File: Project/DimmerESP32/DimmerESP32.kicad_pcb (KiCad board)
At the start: 2 copper layers, 78.7 x 58.4 mm, 14 parts, among them J1 Conn_01x05_Male, J2 Conn_01x04_Male, Q1 BT136-600, U1 MOC3021M, U2 4N25

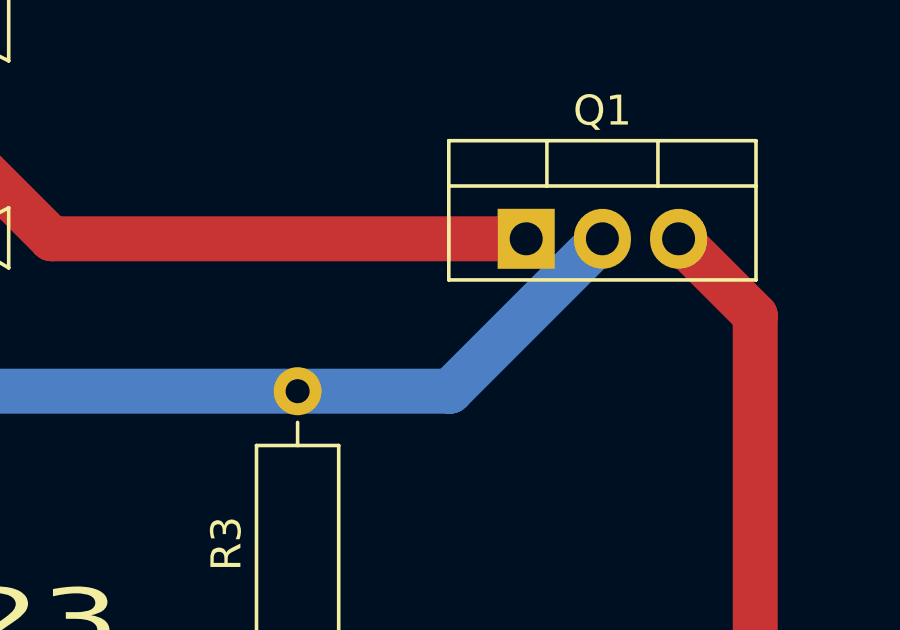
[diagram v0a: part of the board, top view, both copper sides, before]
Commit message: Change 4N25 to TIL111
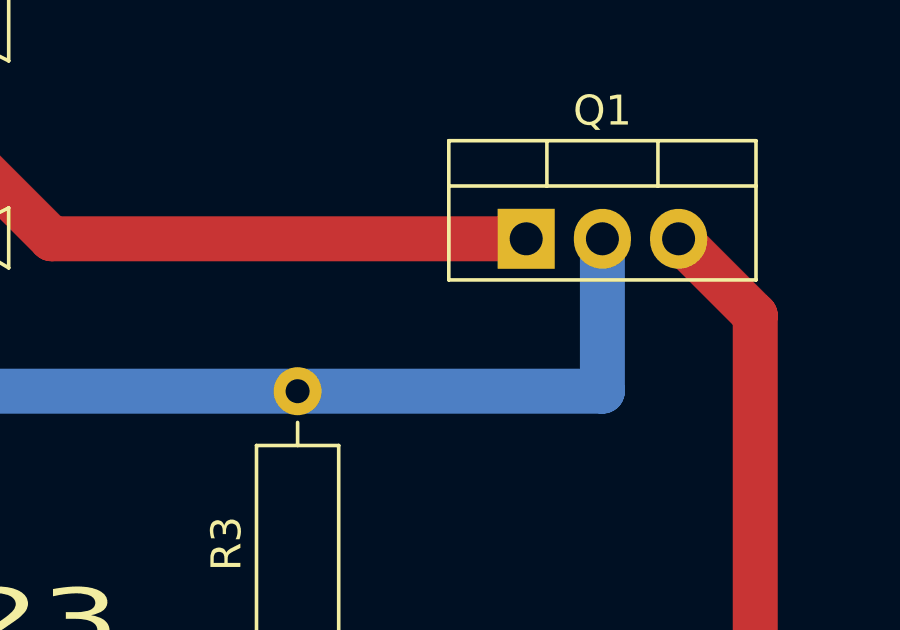
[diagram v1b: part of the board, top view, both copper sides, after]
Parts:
- U2: value 4N25 -> TIL111
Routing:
- net Net-(GridIN1-Pad1): track 76.4 -> 79.4 mm
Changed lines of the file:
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@@
-    )
-  )
-  (footprint "Package_DIP:DIP-6_W7.62mm" (layer "F.Cu")
-    (at 125.74 104.155)
-    (descr "6-lead though-hole mounted DIP package, row spacing 7.62 mm (300 mils)")
-    (tags "THT DIP DIL PDIP 2.54mm 7.62mm 300mil")
-    (property "Sheetfile" "DimmerESP32.kicad_sch")
-    (property "Sheetname" "")
-    (attr through_hole)
-    (fp_text reference "U2" (at 3.81 -2.33) (layer "F.SilkS")
-      (effects (font (size 1 1) (thickness 0.15)))
-    )
-    (fp_text value "4N25" (at 3.81 7.41) (layer "F.Fab")
-      (effects (font (size 1 1) (thickness 0.15)))
-    )
-    (fp_text user "${REFERENCE}" (at 3.81 2.54) (layer "F.Fab")
-      (effects (font (size 1 1) (thickness 0.15)))
-    )
-    (fp_line (start 6.46 6.41) (end 6.46 -1.33) (layer "F.SilkS") (width 0.12))
-    (fp_line (start 2.81 -1.33) (end 1.16 -1.33) (layer "F.SilkS") (width 0.12))
-    (fp_line (start 1.16 6.41) (end 6.46 6.41) (layer "F.SilkS") (width 0.12))
-    (fp_line (start 6.46 -1.33) (end 4.81 -1.33) (layer "F.SilkS") (width 0.12))
-    (fp_line (start 1.16 -1.33) (end 1.16 6.41) (layer "F.SilkS") (width 0.12))
-    (fp_arc (start 4.81 -1.33) (mid 3.81 -0.33) (end 2.81 -1.33) (layer "F.SilkS") (width 0.12))
-    (fp_line (start 8.7 6.6) (end 8.7 -1.55) (layer "F.CrtYd") (width 0.05))
-    (fp_line (start -1.1 6.6) (end 8.7 6.6) (layer "F.CrtYd") (width 0.05))
-    (fp_line (start -1.1 -1.55) (end -1.1 6.6) (layer "F.CrtYd") (width 0.05))
-    (fp_line (start 8.7 -1.55) (end -1.1 -1.55) (layer "F.CrtYd") (width 0.05))
-    (fp_line (start 0.635 -0.27) (end 1.635 -1.27) (layer "F.Fab") (width 0.1))
-    (fp_line (start 6.985 6.35) (end 0.635 6.35) (layer "F.Fab") (width 0.1))
-    (fp_line (start 1.635 -1.27) (end 6.985 -1.27) (layer "F.Fab") (width 0.1))
-    (fp_line (start 0.635 6.35) (end 0.635 -0.27) (layer "F.Fab") (width 0.1))
-    (fp_line (start 6.985 -1.27) (end 6.985 6.35) (layer "F.Fab") (width 0.1))
-    (pad "1" thru_hole rect (at 0 0) (size 1.6 1.6) (drill 0.8) (layers *.Cu *.Mask)
-      (net 1 "Net-(D2-Pad1)") (pintype "passive"))
-    (pad "2" thru_hole oval (at 0 2.54) (size 1.6 1.6) (drill 0.8) (layers *.Cu *.Mask)
-      (net 3 "Net-(D2-Pad3)") (pintype "passive"))
-    (pad "3" thru_hole oval (at 0 5.08) (size 1.6 1.6) (drill 0.8) (layers *.Cu *.Mask)
-      (net 13 "unconnected-(U2-Pad3)") (pinfunction "NC") (pintype "no_connect"))
-    (pad "4" thru_hole oval (at 7.62 5.08) (size 1.6 1.6) (drill 0.8) (layers *.Cu *.Mask)
-      (net 14 "GND") (pintype "passive"))
-    (pad "5" thru_hole oval (at 7.62 2.54) (size 1.6 1.6) (drill 0.8) (layers *.Cu *.Mask)
-      (net 15 "ZeroCrossing") (pintype "passive"))
-    (pad "6" thru_hole oval (at 7.62 0) (size 1.6 1.6) (drill 0.8) (layers *.Cu *.Mask)
-      (net 16 "unconnected-(U2-Pad6)") (pintype "passive"))
-    (model "${KICAD6_3DMODEL_DIR}/Package_DIP.3dshapes/DIP-6_W7.62mm.wrl"
-      (offset (xyz 0 0 0))
-      (scale (xyz 1 1 1))
-      (rotate (xyz 0 0 0))
     )
   )
@@
     )
   )
+  (footprint "Package_DIP:DIP-6_W7.62mm" (layer "F.Cu")
+    (at 125.74 104.155)
+    (descr "6-lead though-hole mounted DIP package, row spacing 7.62 mm (300 mils)")
+    (tags "THT DIP DIL PDIP 2.54mm 7.62mm 300mil")
+    (property "Sheetfile" "DimmerESP32.kicad_sch")
+    (property "Sheetname" "")
+    (attr through_hole)
+    (fp_text reference "U2" (at 3.81 -2.33) (layer "F.SilkS")
+      (effects (font (size 1 1) (thickness 0.15)))
+    )
+    (fp_text value "TIL111" (at 3.81 7.41) (layer "F.Fab")
+      (effects (font (size 1 1) (thickness 0.15)))
+    )
+    (fp_text user "${REFERENCE}" (at 3.81 2.54) (layer "F.Fab")
+      (effects (font (size 1 1) (thickness 0.15)))
+    )
+    (fp_line (start 1.16 6.41) (end 6.46 6.41) (layer "F.SilkS") (width 0.12))
+    (fp_line (start 6.46 6.41) (end 6.46 -1.33) (layer "F.SilkS") (width 0.12))
+    (fp_line (start 1.16 -1.33) (end 1.16 6.41) (layer "F.SilkS") (width 0.12))
+    (fp_line (start 2.81 -1.33) (end 1.16 -1.33) (layer "F.SilkS") (width 0.12))
+    (fp_line (start 6.46 -1.33) (end 4.81 -1.33) (layer "F.SilkS") (width 0.12))
+    (fp_arc (start 4.81 -1.33) (mid 3.81 -0.33) (end 2.81 -1.33) (layer "F.SilkS") (width 0.12))
+    (fp_line (start -1.1 6.6) (end 8.7 6.6) (layer "F.CrtYd") (width 0.05))
+    (fp_line (start 8.7 6.6) (end 8.7 -1.55) (layer "F.CrtYd") (width 0.05))
+    (fp_line (start -1.1 -1.55) (end -1.1 6.6) (layer "F.CrtYd") (width 0.05))
+    (fp_line (start 8.7 -1.55) (end -1.1 -1.55) (layer "F.CrtYd") (width 0.05))
+    (fp_line (start 6.985 -1.27) (end 6.985 6.35) (layer "F.Fab") (width 0.1))
+    (fp_line (start 0.635 6.35) (end 0.635 -0.27) (layer "F.Fab") (width 0.1))
+    (fp_line (start 0.635 -0.27) (end 1.635 -1.27) (layer "F.Fab") (width 0.1))
+    (fp_line (start 6.985 6.35) (end 0.635 6.35) (layer "F.Fab") (width 0.1))
+    (fp_line (start 1.635 -1.27) (end 6.985 -1.27) (layer "F.Fab") (width 0.1))
+    (pad "1" thru_hole rect (at 0 0) (size 1.6 1.6) (drill 0.8) (layers *.Cu *.Mask)
+      (net 1 "Net-(D2-Pad1)") (pintype "passive"))
+    (pad "2" thru_hole oval (at 0 2.54) (size 1.6 1.6) (drill 0.8) (layers *.Cu *.Mask)
+      (net 3 "Net-(D2-Pad3)") (pintype "passive"))
+    (pad "3" thru_hole oval (at 0 5.08) (size 1.6 1.6) (drill 0.8) (layers *.Cu *.Mask)
+      (net 13 "unconnected-(U2-Pad3)") (pinfunction "NC") (pintype "no_connect"))
+    (pad "4" thru_hole oval (at 7.62 5.08) (size 1.6 1.6) (drill 0.8) (layers *.Cu *.Mask)
+      (net 14 "GND") (pintype "passive"))
+    (pad "5" thru_hole oval (at 7.62 2.54) (size 1.6 1.6) (drill 0.8) (layers *.Cu *.Mask)
+      (net 15 "ZeroCrossing") (pintype "passive"))
+    (pad "6" thru_hole oval (at 7.62 0) (size 1.6 1.6) (drill 0.8) (layers *.Cu *.Mask)
+      (net 16 "unconnected-(U2-Pad6)") (pintype "passive"))
+    (model "${KICAD6_3DMODEL_DIR}/Package_DIP.3dshapes/DIP-6_W7.62mm.wrl"
+      (offset (xyz 0 0 0))
+      (scale (xyz 1 1 1))
+      (rotate (xyz 0 0 0))
+    )
+  )
   (gr_rect (start 182.88 92.695) (end 129.55 114.3) (layer "F.SilkS") (width 0.15) (fill none))
   (gr_rect (start 104.14 55.88) (end 182.88 114.3) (layer "Edge.Cuts") (width 0.1) (fill none))
@@
   (segment (start 109.3 63.9) (end 109.3 76.12) (width 1.5) (layer "F.Cu") (net 11))
   (segment (start 109.3 76.12) (end 109.22 76.2) (width 0.25) (layer "F.Cu") (net 11))
-  (segment (start 160.02 73.66) (end 165.1 73.66) (width 1.5) (layer "B.Cu") (net 11))
+  (segment (start 170.18 73.66) (end 170.18 68.58) (width 1.5) (layer "B.Cu") (net 11))
+  (segment (start 160.02 73.66) (end 170.18 73.66) (width 1.5) (layer "B.Cu") (net 11))
   (segment (start 109.22 76.2) (end 111.76 73.66) (width 1.5) (layer "B.Cu") (net 11))
-  (segment (start 165.1 73.66) (end 170.18 68.58) (width 1.5) (layer "B.Cu") (net 11))
   (segment (start 111.76 73.66) (end 160.02 73.66) (width 1.5) (layer "B.Cu") (net 11))
   (segment (start 175.275 71.135) (end 172.72 68.58) (width 1.5) (layer "F.Cu") (net 12))

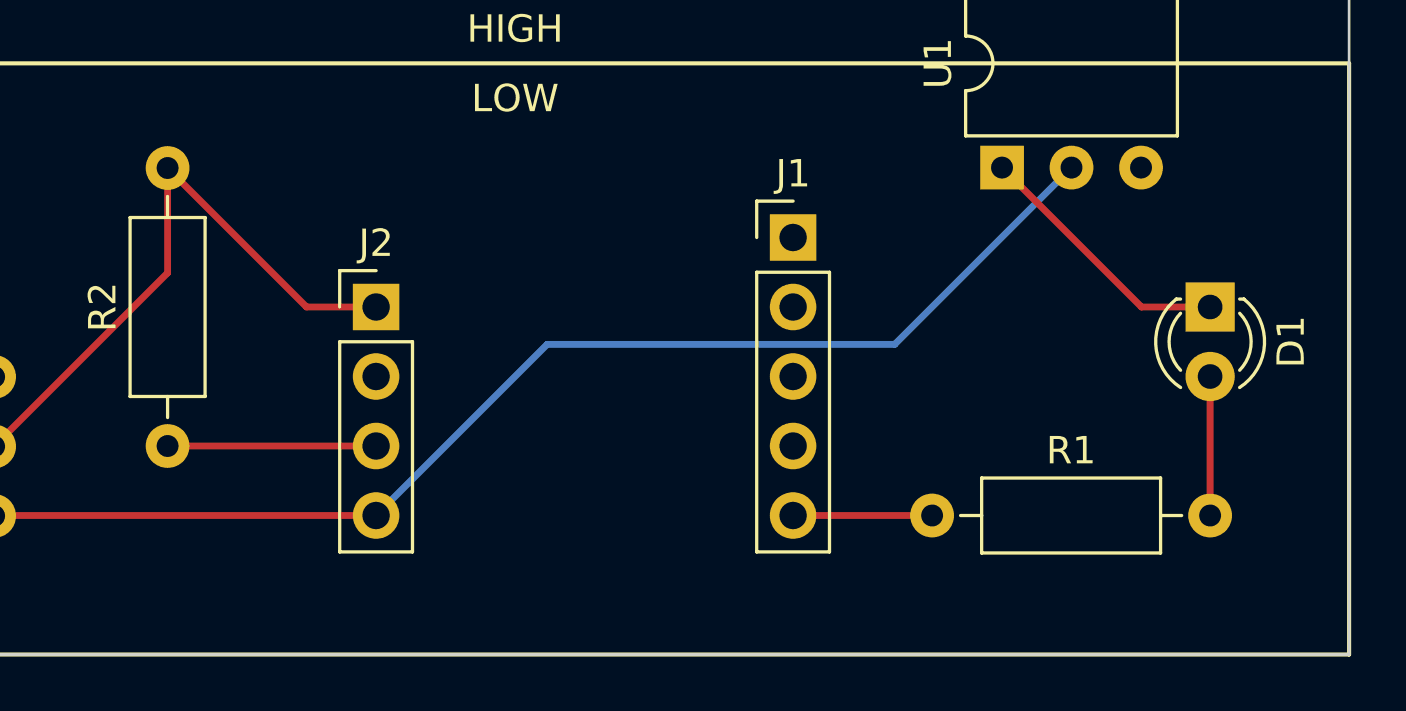
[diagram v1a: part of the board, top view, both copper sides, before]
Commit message: Remove LED and resistor from schem and PCB
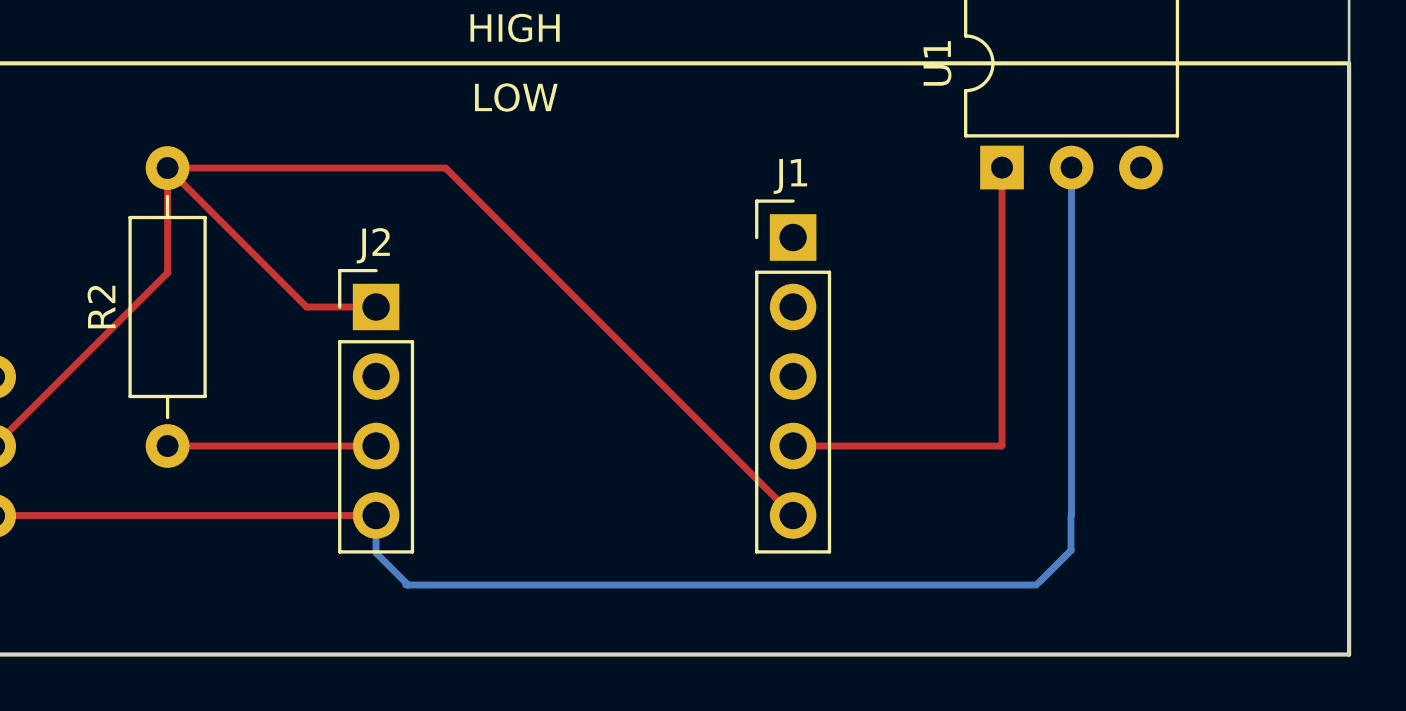
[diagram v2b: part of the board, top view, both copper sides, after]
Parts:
- removed D1: LED, LED_THT:LED_D3.0mm
- removed R1: 200, Resistor_THT:R_Axial_DIN0207_L6.3mm_D2.5mm_P10.16mm_Horizontal
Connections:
- J1 pad 4: unconnected-(J1-Pad4) -> DimmerSignal
- J1 pad 5: DimmerSignal -> ZeroCrossing
- J2 pad 1: ZeroCrossing -> unconnected-(J2-Pad1)
- U1 pad 1: Net-(D1-Pad1) -> DimmerSignal
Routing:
- net ZeroCrossing: track 22.5 -> 50.6 mm
- net DimmerSignal: track 5.08 -> 17.8 mm
- net GND: track 44.6 -> 55.7 mm
- net Net-(D1-Pad1): track 9.72 -> 0.00 mm
- net Net-(D1-Pad2): track 5.08 -> 0.00 mm
